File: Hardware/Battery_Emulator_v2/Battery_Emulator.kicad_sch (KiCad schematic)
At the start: 23 parts, among them J1 Vin, J2 USB4105-GF-A-060, J3 Cell1_Vout, U10 ATmega328PB-A, U3 74AHC2G125DP,125, U4 FT230XS-R, U9 KA78M05_TO252, Y1 Crystal_GND24

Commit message: Modified the v2 pcb
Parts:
- added J4: Cell1_Vout, TerminalBlock_Phoenix:TerminalBlock_Phoenix_MKDS-1,5-2-5.08_1x02_P5.08mm_Horizontal, symbol Connector:Screw_Terminal_01x02
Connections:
- new net Cell_2/COUT+: J4.1 (Pin_1)
- new net Cell_2/COUT-: J4.2 (Pin_2)
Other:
- added sheet Cell_2 (Cell_1.kicad_sch)
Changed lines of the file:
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@@
+    (stroke (width 0) (type default))
+  )
+  (wire (pts (xy 220.98 72.136) (xy 226.06 72.136))
     (stroke (width 0) (type default))
   )
@@
     (stroke (width 0) (type default))
   )
+  (wire (pts (xy 220.98 81.026) (xy 226.06 81.026))
+    (stroke (width 0) (type default))
+  )
   (wire (pts (xy 106.045 193.04) (xy 107.315 193.04))
     (stroke (width 0) (type default))
@@
     (stroke (width 0) (type default))
   )
+  (wire (pts (xy 285.75 64.516) (xy 292.735 64.516))
+    (stroke (width 0) (type default))
+  )
   (wire (pts (xy 91.44 120.65) (xy 94.615 120.65))
     (stroke (width 0) (type default))
@@
     (stroke (width 0) (type default))
   )
+  (wire (pts (xy 285.75 67.056) (xy 292.735 67.056))
+    (stroke (width 0) (type default))
+  )
   (wire (pts (xy 43.18 166.37) (xy 50.165 166.37))
     (stroke (width 0) (type default))
@@
     (stroke (width 0) (type default))
   )
+  (wire (pts (xy 220.98 74.676) (xy 226.06 74.676))
+    (stroke (width 0) (type default))
+  )
+  (wire (pts (xy 220.98 65.786) (xy 226.06 65.786))
+    (stroke (width 0) (type default))
+  )
   (wire (pts (xy 88.265 199.39) (xy 88.265 200.025))
     (stroke (width 0) (type default))
@@
   )
   (wire (pts (xy 66.675 166.37) (xy 66.675 167.64))
+    (stroke (width 0) (type default))
+  )
+  (wire (pts (xy 220.98 63.246) (xy 226.06 63.246))
     (stroke (width 0) (type default))
   )
@@
     (effects (font (size 1.27 1.27)) (justify left bottom))
   )
+  (label "SDA_cell_1-7" (at 220.98 72.136 180) (fields_autoplaced)
+    (effects (font (size 1.27 1.27)) (justify right bottom))
+  )
+  (label "GND" (at 220.98 81.026 180) (fields_autoplaced)
+    (effects (font (size 1.27 1.27)) (justify right bottom))
+  )
+  (label "SCL" (at 220.98 74.676 180) (fields_autoplaced)
+    (effects (font (size 1.27 1.27)) (justify right bottom))
+  )
   (label "D+" (at 55.245 114.3 0) (fields_autoplaced)
     (effects (font (size 1.27 1.27)) (justify left bottom))
@@
     (effects (font (size 1.27 1.27)) (justify left bottom))
   )
+  (label "+12V" (at 220.98 63.246 180) (fields_autoplaced)
+    (effects (font (size 1.27 1.27)) (justify right bottom))
+  )
   (label "SCL" (at 220.98 43.18 180) (fields_autoplaced)
     (effects (font (size 1.27 1.27)) (justify right bottom))
@@
   )
   (label "GND" (at 220.98 49.53 180) (fields_autoplaced)
+    (effects (font (size 1.27 1.27)) (justify right bottom))
+  )
+  (label "+5V" (at 220.98 65.786 180) (fields_autoplaced)
     (effects (font (size 1.27 1.27)) (justify right bottom))
   )
@@
     )
   )
+  (symbol (lib_id "Connector:Screw_Terminal_01x02") (at 297.815 64.516 0) (unit 1)
+    (in_bom yes) (on_board yes) (dnp no)
+    (property "Reference" "J4" (at 300.355 64.516 0)
+      (effects (font (size 1.27 1.27)) (justify left))
+    )
+    (property "Value" "Cell1_Vout" (at 300.355 67.056 0)
+      (effects (font (size 1.27 1.27)) (justify left))
+    )
+    (property "Footprint" "TerminalBlock_Phoenix:TerminalBlock_Phoenix_MKDS-1,5-2-5.08_1x02_P5.08mm_Horizontal" (at 297.815 64.516 0)
+      (effects (font (size 1.27 1.27)) hide)
+    )
+    (property "Datasheet" "~" (at 297.815 64.516 0)
+      (effects (font (size 1.27 1.27)) hide)
+    )
+    (pin "1")
+    (pin "2")
+    (instances
+      (project "Battery_Emulator"
+        (path "/bb7641ff-0dfd-4f4a-b3be-57afbbb9fdac"
+          (reference "J4") (unit 1)
+        )
+      )
+    )
+  )
   (symbol (lib_id "Device:Crystal_GND24") (at 96.52 187.325 90) (unit 1)
     (in_bom yes) (on_board yes) (dnp no)
@@
       )
     )
+  )
+  (sheet (at 226.06 59.436) (size 59.69 25.4) (fields_autoplaced)
+    (stroke (width 0.1524) (type solid))
+    (fill (color 0 0 0 0.0000))
+    (property "Sheetname" "Cell_2" (at 226.06 58.7244 0)
+      (effects (font (size 1.27 1.27)) (justify left bottom))
+    )
+    (property "Sheetfile" "Cell_1.kicad_sch" (at 226.06 85.4206 0)
+      (effects (font (size 1.27 1.27)) (justify left top))
+    )
+    (pin "+12V" input (at 226.06 63.246 180)
+      (effects (font (size 1.27 1.27)) (justify left))
+    )
+    (pin "GND" input (at 226.06 81.026 180)
+      (effects (font (size 1.27 1.27)) (justify left))
+    )
+    (pin "COUT+" output (at 285.75 64.516 0)
+      (effects (font (size 1.27 1.27)) (justify right))
+    )
+    (pin "COUT-" output (at 285.75 67.056 0)
+      (effects (font (size 1.27 1.27)) (justify right))
+    )
+    (pin "+5V" input (at 226.06 65.786 180)
+      (effects (font (size 1.27 1.27)) (justify left))
+    )
+    (pin "SDA" input (at 226.06 72.136 180)
+      (effects (font (size 1.27 1.27)) (justify left))
+    )
+    (pin "SCL" input (at 226.06 74.676 180)
+      (effects (font (size 1.27 1.27)) (justify left))
+    )
+    (instances
+      (project "Battery_Emulator"
+        (path "/bb7641ff-0dfd-4f4a-b3be-57afbbb9fdac" (page "3"))
+      )
+    )

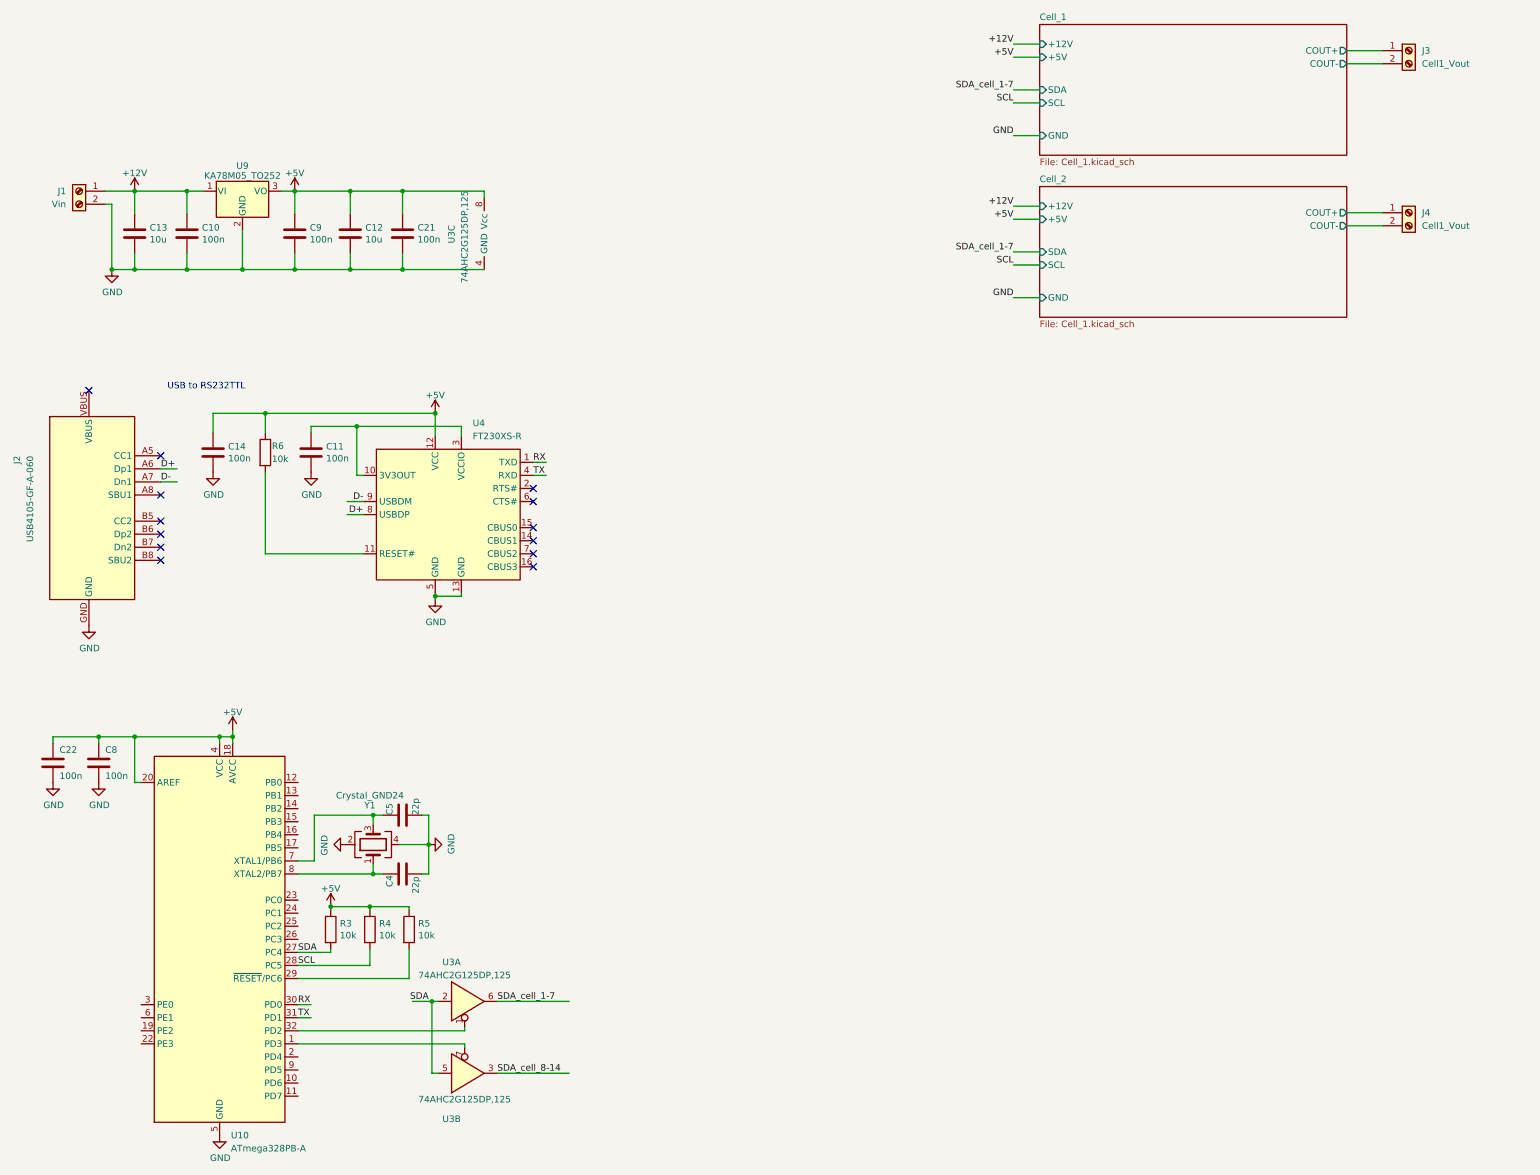
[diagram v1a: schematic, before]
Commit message: Hardware Update
V2 with four cells with the same layout
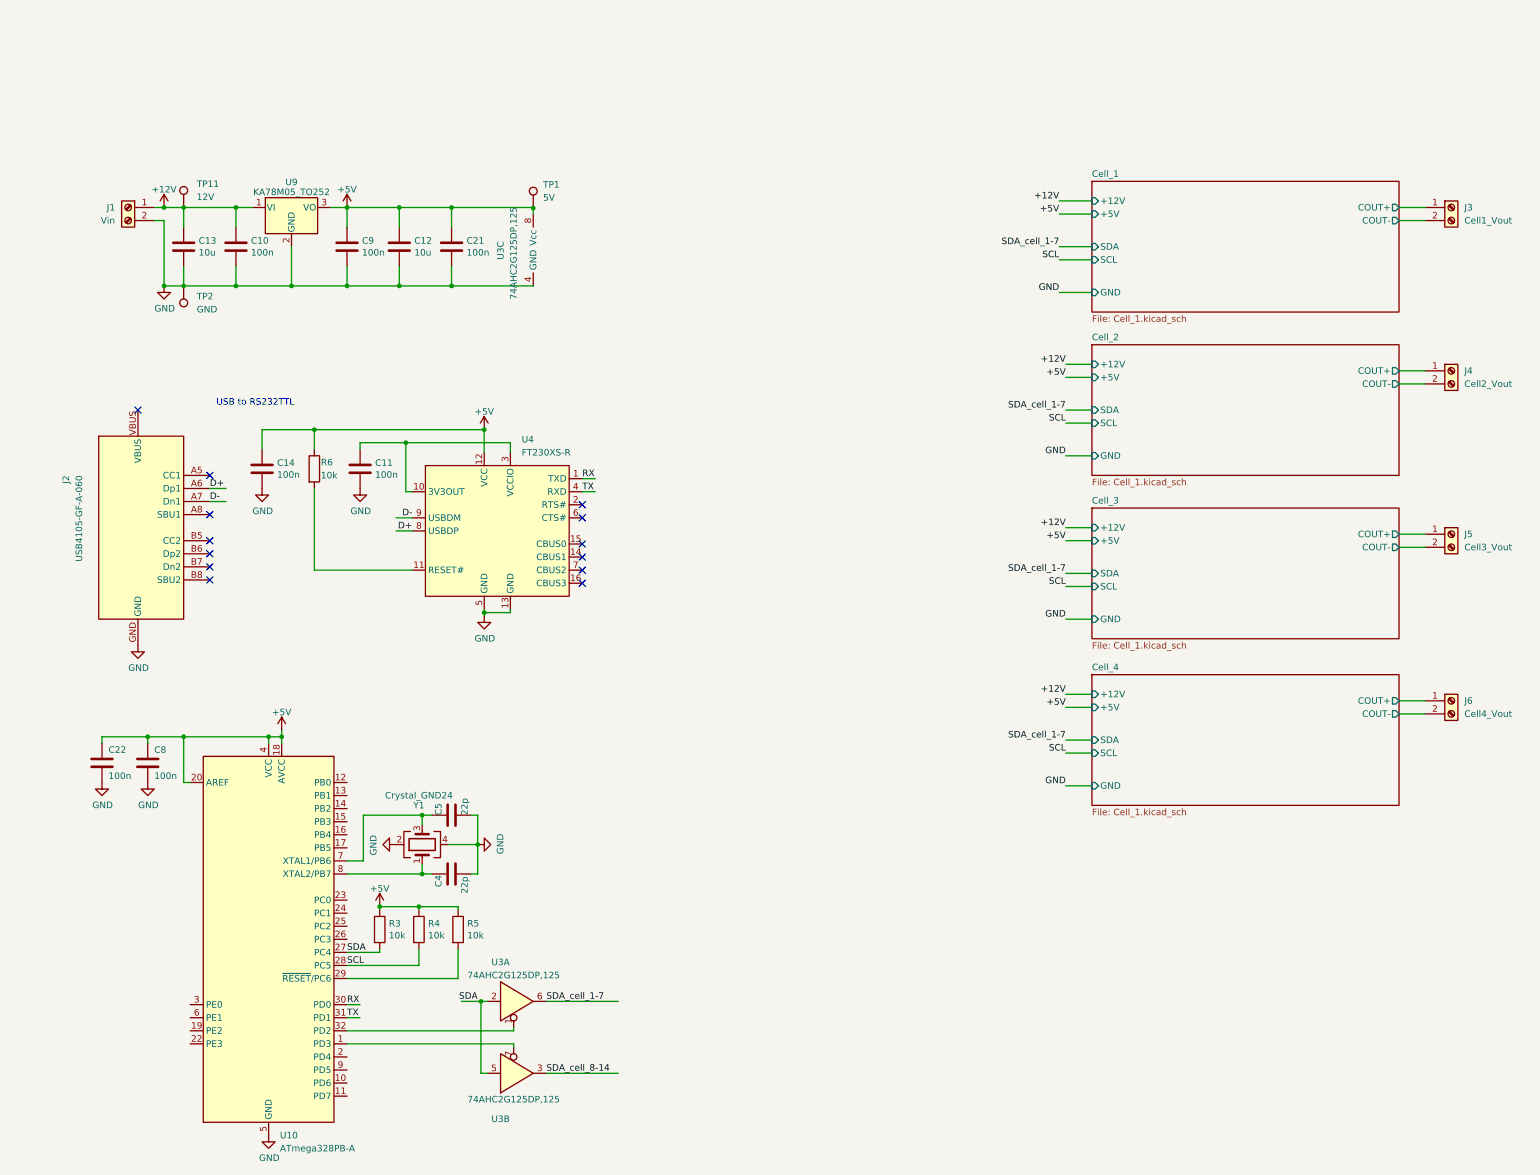
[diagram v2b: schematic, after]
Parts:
- added J5: Cell3_Vout, TerminalBlock_Phoenix:TerminalBlock_Phoenix_MKDS-1,5-2-5.08_1x02_P5.08mm_Horizontal, symbol Connector:Screw_Terminal_01x02
- added J6: Cell4_Vout, TerminalBlock_Phoenix:TerminalBlock_Phoenix_MKDS-1,5-2-5.08_1x02_P5.08mm_Horizontal, symbol Connector:Screw_Terminal_01x02
- added TP1: 5V, TestPoint:TestPoint_Pad_D2.5mm, symbol Connector:TestPoint
- added TP11: 12V, TestPoint:TestPoint_Pad_D2.5mm, symbol Connector:TestPoint
- added TP2: GND, TestPoint:TestPoint_Pad_D2.5mm, symbol Connector:TestPoint
- J4: value Cell1_Vout -> Cell2_Vout
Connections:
- net +12V: now also TP11.1
- net +5V: now also TP1.1
- net GND: now also TP2.1
- new net Cell_3/COUT+: J5.1 (Pin_1)
- new net Cell_3/COUT-: J5.2 (Pin_2)
- new net Cell_4/COUT+: J6.1 (Pin_1)
- new net Cell_4/COUT-: J6.2 (Pin_2)
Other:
- added sheet Cell_3 (Cell_1.kicad_sch)
- added sheet Cell_4 (Cell_1.kicad_sch)
- moved on the sheet: C10, C11, C12, C13, C14, C21, C22, C4, C5, C8, C9, J1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
